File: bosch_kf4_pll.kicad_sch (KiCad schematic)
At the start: 13 parts, among them J1 Conn_ARM_SWD_TagConnect_TC203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, J2 CPD18U42CD, J4 audio, Q2 AO3400A, U1 CH32V003F4U6

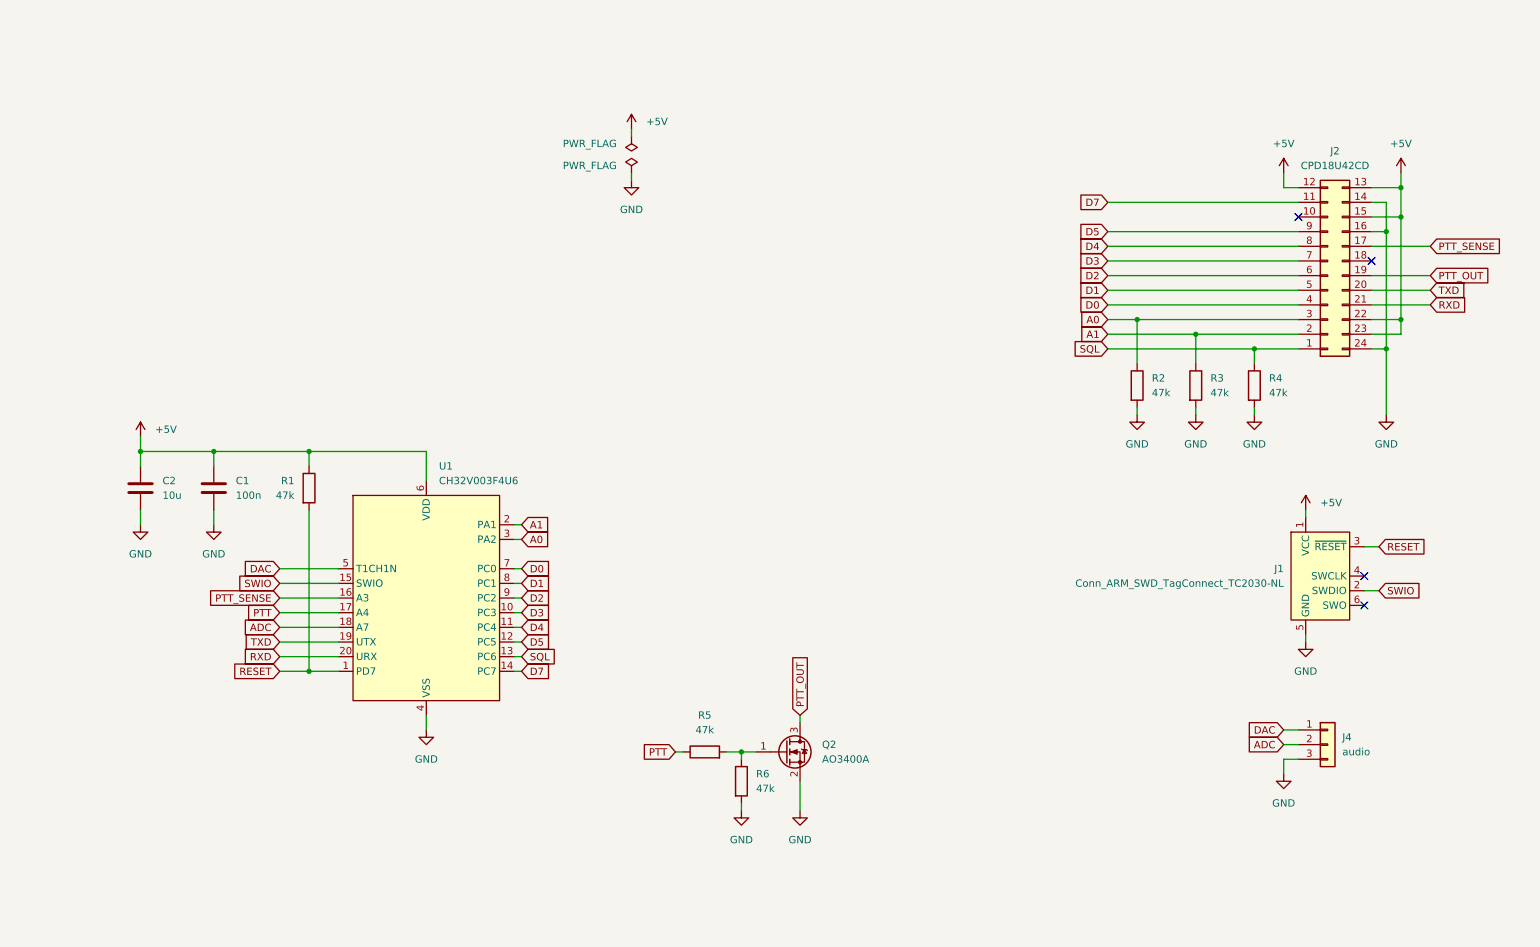
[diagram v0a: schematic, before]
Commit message: Added CTCSS filters
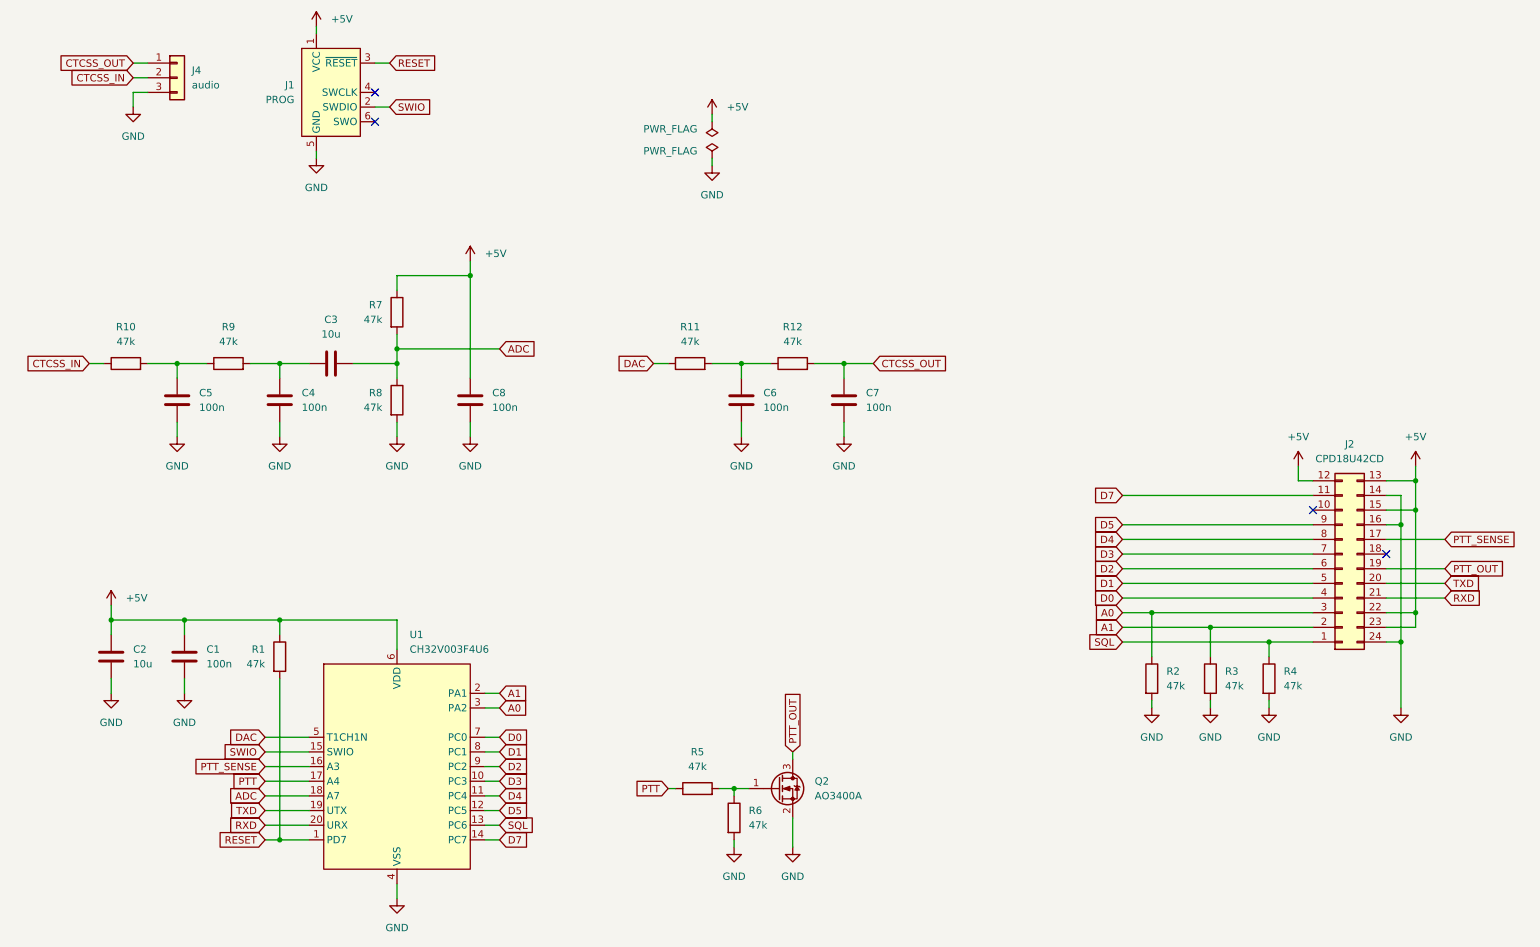
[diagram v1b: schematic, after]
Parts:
- added C3: 10u, Capacitor_SMD:C_0603_1608Metric, symbol Device:C
- added C4, C5, C6, C7, C8: 100n, Capacitor_SMD:C_0603_1608Metric, symbol Device:C
- added R10, R11, R12, R7, R8, R9: 47k, Resistor_SMD:R_0603_1608Metric, symbol Device:R
- J1: value Conn_ARM_SWD_TagConnect_TC2030-NL -> PROG
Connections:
- net +5V: now also C8.1, R7.1
- net ADC: now also C3.2, R7.2, R8.1; no longer J4.2 (Pin_2)
- net DAC: now also R11.1; no longer J4.1 (Pin_1)
- net GND: now also C4.2, C5.2, C6.2, C7.2, C8.2, R8.2
- new net: C3.1, C4.1, R9.2
- new net: C5.1, R10.2, R9.1
- new net: C6.1, R11.2, R12.1
- new net CTCSS_IN: J4.2 (Pin_2), R10.1
- new net CTCSS_OUT: C7.1, J4.1 (Pin_1), R12.2
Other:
- moved on the sheet: C1, C2, J1, J2, J4, Q2, R1, R2, R3, R4, R5, R6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

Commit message: Finalized Rev2, added gerbers and PDF schematic
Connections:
- net CTCSS_OUT: now also J4.3 (Pin_3); no longer J4.1 (Pin_1)
- net GND: now also J4.1 (Pin_1); no longer J4.3 (Pin_3)
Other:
- company: CommSplice.com -> RobinOlejnik.com
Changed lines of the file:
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@@
   (title_block
     (title "Bosch KF164 PLL EPROM Replacement")
-    (date "2023-11-17")
+    (date "2023-11-23")
     (rev "2")
-    (company "CommSplice.com")
+    (company "RobinOlejnik.com")
     (comment 1 "Robin Olejnik")
   )
@@
     (stroke (width 0) (type default))
   )
+  (wire (pts (xy 36.83 27.94) (xy 39.37 27.94))
+    (stroke (width 0) (type default))
+  )
   (wire (pts (xy 82.55 80.01) (xy 82.55 82.55))
     (stroke (width 0) (type default))
@@
     (stroke (width 0) (type default))
   )
-  (wire (pts (xy 36.83 27.94) (xy 39.37 27.94))
-    (stroke (width 0) (type default))
-  )
   (wire (pts (xy 62.23 90.17) (xy 62.23 92.71))
     (stroke (width 0) (type default))
@@
     (stroke (width 0) (type default))
   )
-  (wire (pts (xy 39.37 33.02) (xy 36.83 33.02))
-    (stroke (width 0) (type default))
-  )
   (wire (pts (xy 233.68 139.7) (xy 233.68 138.43))
     (stroke (width 0) (type default))
@@
   )
   (wire (pts (xy 256.54 128.27) (xy 254 128.27))
+    (stroke (width 0) (type default))
+  )
+  (wire (pts (xy 36.83 33.02) (xy 39.37 33.02))
     (stroke (width 0) (type default))
   )
@@
     )
   )
-  (symbol (lib_id "Connector_Generic:Conn_01x03") (at 44.45 30.48 0) (unit 1)
-    (in_bom yes) (on_board yes) (dnp no) (fields_autoplaced)
-    (property "Reference" "J4" (at 46.99 29.21 0)
-      (effects (font (size 1.27 1.27)) (justify left))
-    )
-    (property "Value" "audio" (at 46.99 31.75 0)
-      (effects (font (size 1.27 1.27)) (justify left))
-    )
+  (symbol (lib_id "Connector_Generic:Conn_01x03") (at 44.45 30.48 0) (mirror x) (unit 1)
+    (in_bom yes) (on_board yes) (dnp no)
+    (property "Reference" "J4" (at 46.99 31.75 0)
+      (effects (font (size 1.27 1.27)) (justify left))
+    )
+    (property "Value" "audio" (at 46.99 29.21 0)
+      (effects (font (size 1.27 1.27)) (justify left))
+    )
